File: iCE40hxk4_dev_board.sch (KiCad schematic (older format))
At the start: 0 parts

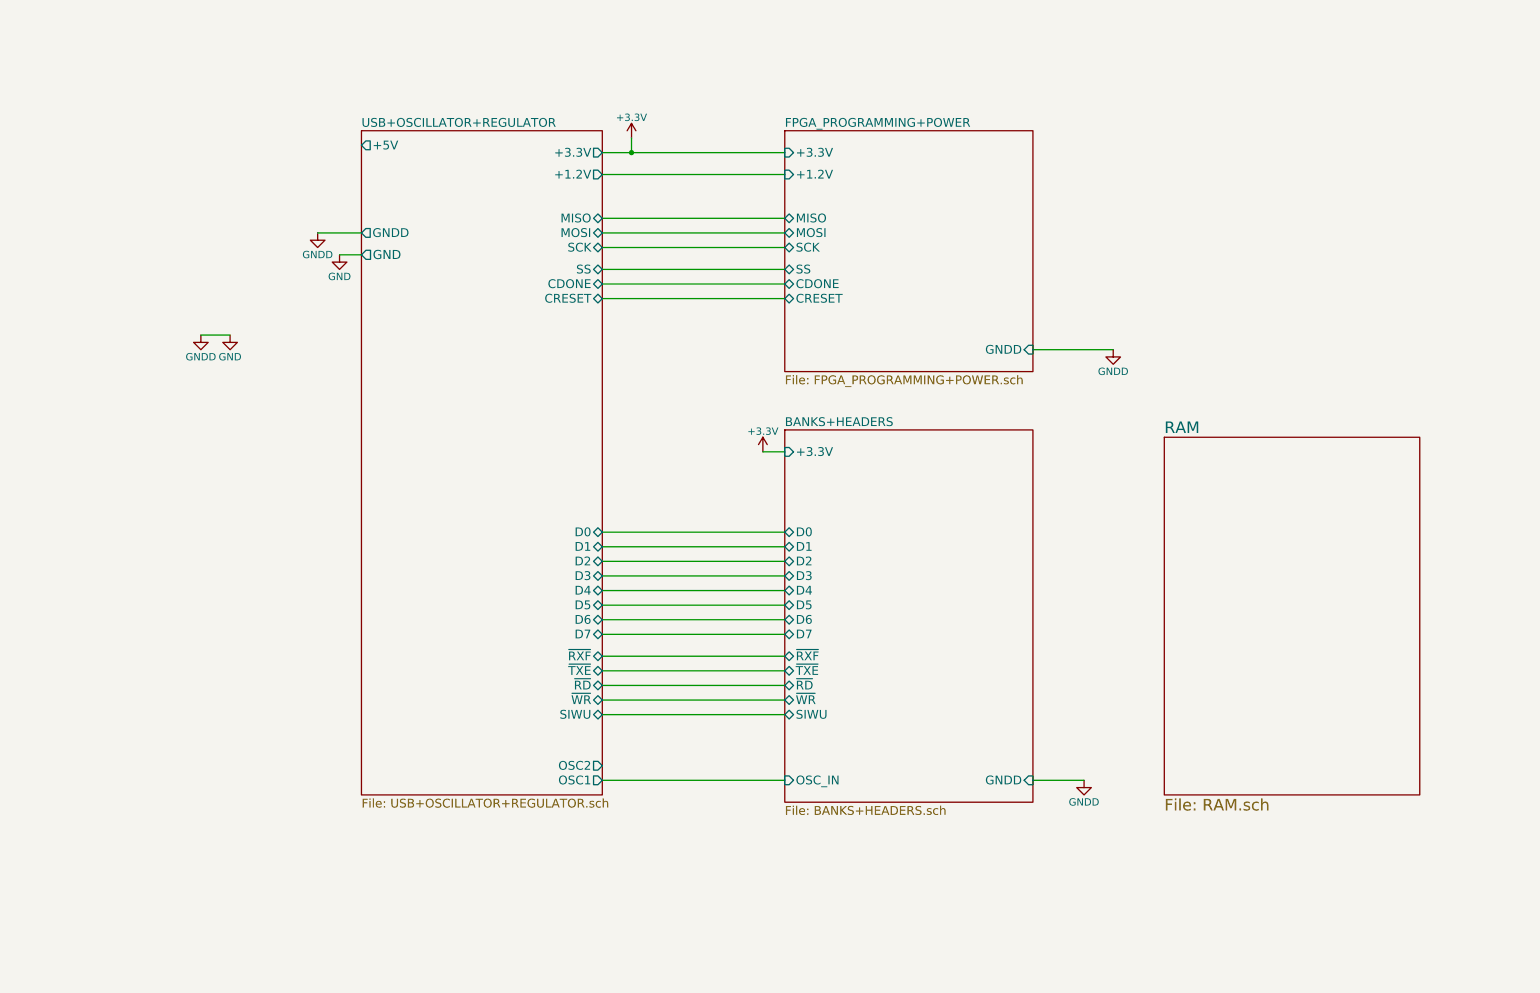
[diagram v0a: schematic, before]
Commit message: Reordered connections again. Option 1: RAM at left bank, some connections at left and top banks.
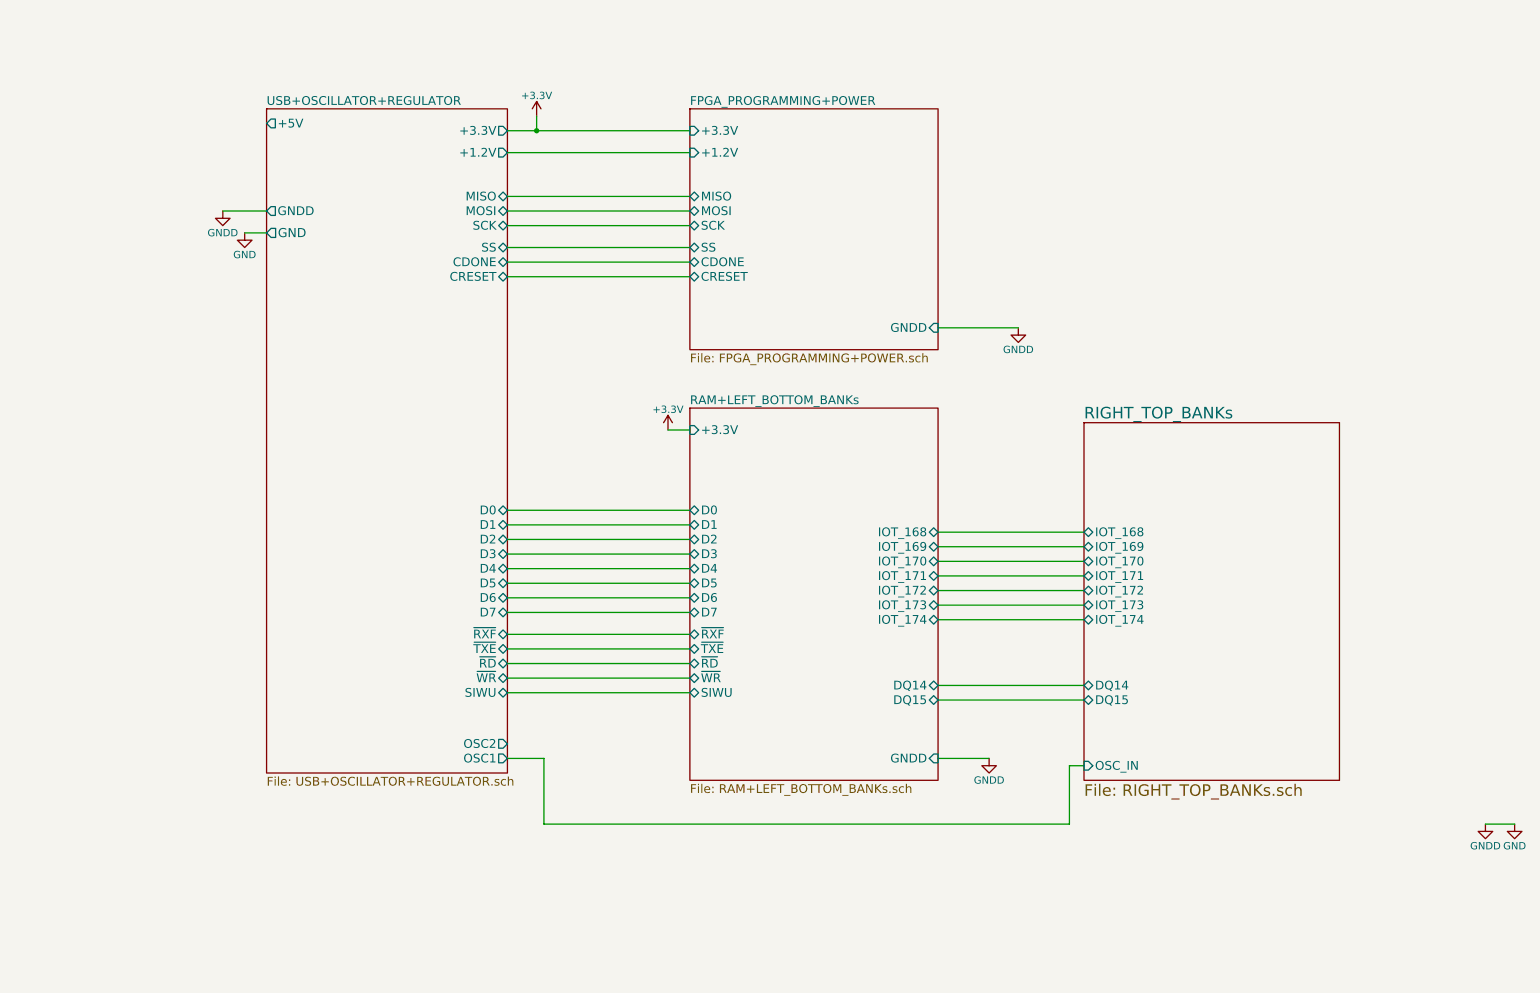
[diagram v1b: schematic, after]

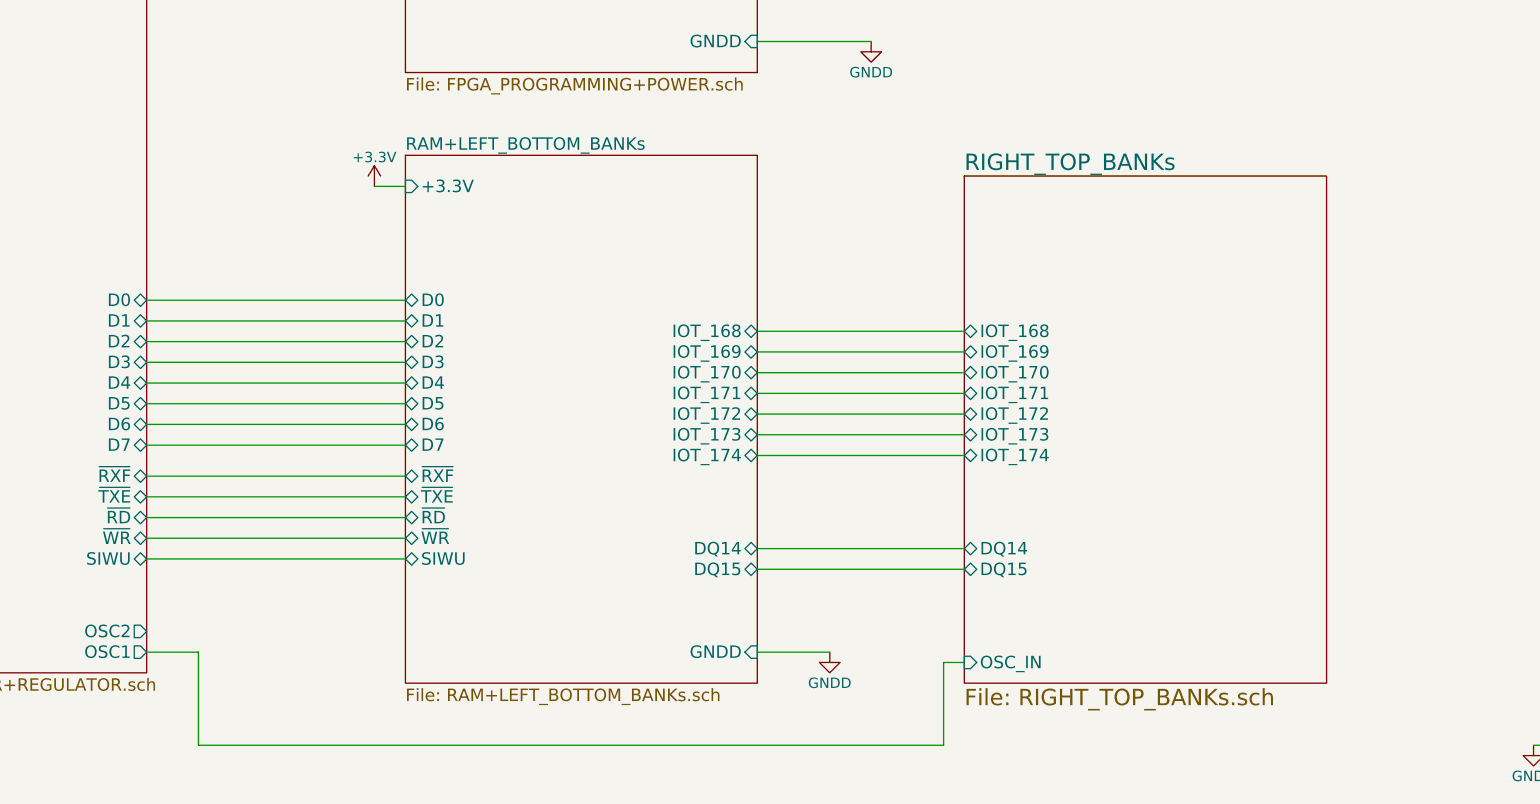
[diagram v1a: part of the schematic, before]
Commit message: The schematic is now free of any ERC error. Not connected and power flags added. No more global power pins, hierarchical labels used for power connections. TODO list: -Check if all footpritns are already assigned. -Export a BOM list, and check if all part numbers are assigned. -Add leds and testpoints. -Make another branch, with the RAM connections to the left and right banks, so the ram could be located in the bottom layer and the FPGA in the top layer. -Reorder the connections of the current branch if necessary, do the placement of components and ground planes.
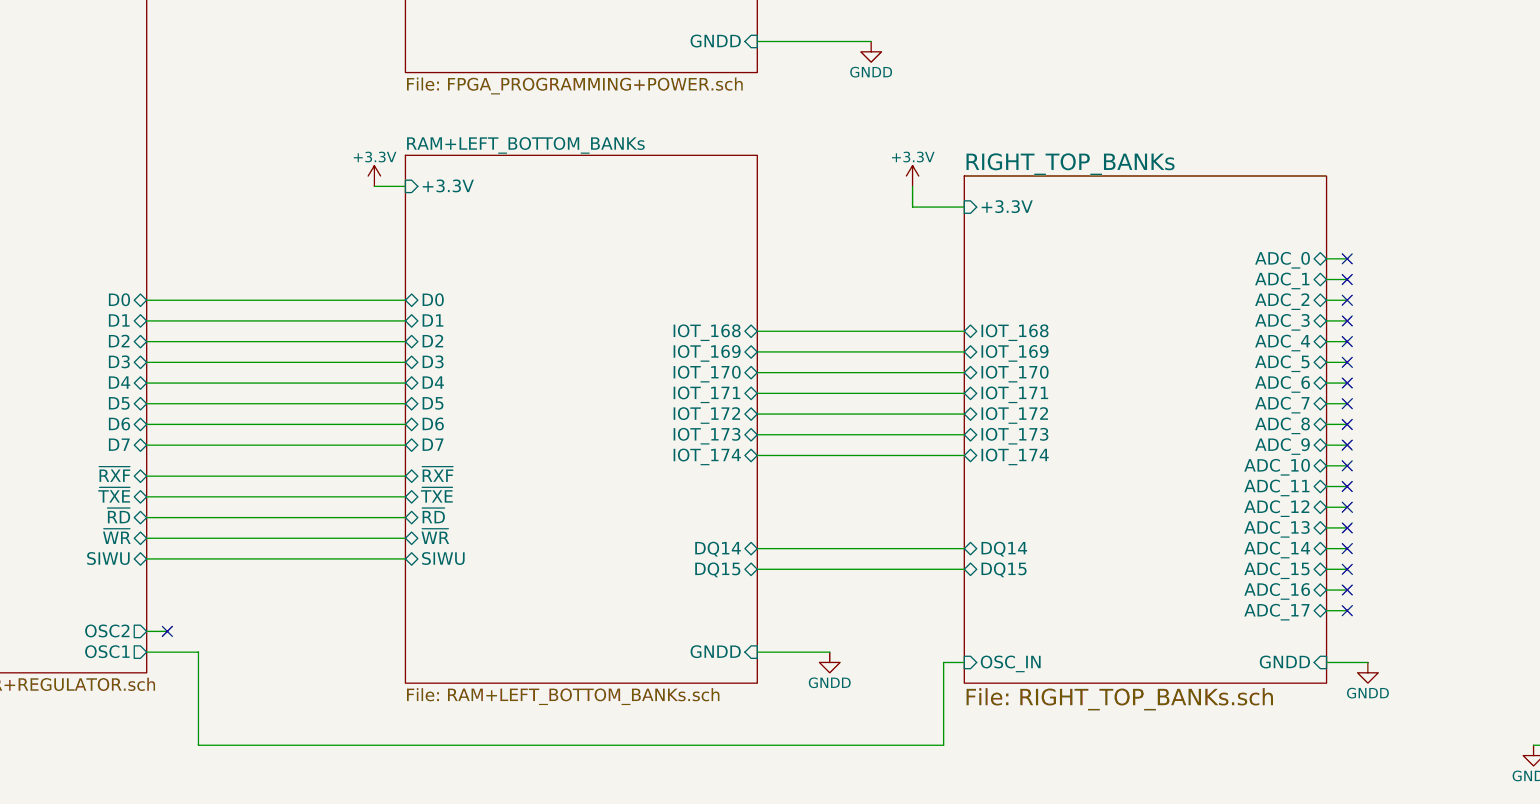
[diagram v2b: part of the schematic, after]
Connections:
- no-connect marks 0 -> 19
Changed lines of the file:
@@
 F10 "DQ15" B L 7850 5250 60
 F11 "DQ14" B L 7850 5150 60
+F12 "ADC_0" B R 9600 3750 60
+F13 "ADC_1" B R 9600 3850 60
+F14 "ADC_2" B R 9600 3950 60
+F15 "ADC_3" B R 9600 4050 60
+F16 "ADC_4" B R 9600 4150 60
+F17 "ADC_5" B R 9600 4250 60
+F18 "ADC_6" B R 9600 4350 60
+F19 "ADC_7" B R 9600 4450 60
+F20 "ADC_8" B R 9600 4550 60
+F21 "ADC_9" B R 9600 4650 60
+F22 "ADC_10" B R 9600 4750 60
+F23 "ADC_11" B R 9600 4850 60
+F24 "ADC_12" B R 9600 4950 60
+F25 "ADC_13" B R 9600 5050 60
+F26 "ADC_14" B R 9600 5150 60
+F27 "ADC_15" B R 9600 5250 60
+F28 "ADC_16" B R 9600 5350 60
+F29 "ADC_17" B R 9600 5450 60
+F30 "+3.3V" I L 7850 3500 60
+F31 "GNDD" I R 9600 5700 60
 $EndSheet
 Wire Wire Line
@@
 Wire Wire Line
 	6850 5150 7850 5150
+Wire Wire Line
+	9600 3750 9700 3750
+Wire Wire Line
+	9600 3850 9700 3850
+Wire Wire Line
+	9600 3950 9700 3950
+Wire Wire Line
+	9600 4050 9700 4050
+Wire Wire Line
+	9600 4150 9700 4150
+Wire Wire Line
+	9600 4250 9700 4250
+Wire Wire Line
+	9600 4350 9700 4350
+Wire Wire Line
+	9600 4450 9700 4450
+Wire Wire Line
+	9600 4550 9700 4550
+Wire Wire Line
+	9600 4650 9700 4650
+Wire Wire Line
+	9600 4750 9700 4750
+Wire Wire Line
+	9600 4850 9700 4850
+Wire Wire Line
+	9600 4950 9700 4950
+Wire Wire Line
+	9600 5050 9700 5050
+Wire Wire Line
+	9600 5150 9700 5150
+Wire Wire Line
+	9600 5250 9700 5250
+Wire Wire Line
+	9600 5350 9700 5350
+Wire Wire Line
+	9600 5450 9700 5450
+NoConn ~ 9700 3750
+NoConn ~ 9700 3850
+NoConn ~ 9700 3950
+NoConn ~ 9700 4050
+NoConn ~ 9700 4150
+NoConn ~ 9700 4250
+NoConn ~ 9700 4350
+NoConn ~ 9700 4450
+NoConn ~ 9700 4550
+NoConn ~ 9700 4650
+NoConn ~ 9700 4750
+NoConn ~ 9700 4850
+NoConn ~ 9700 4950
+NoConn ~ 9700 5050
+NoConn ~ 9700 5150
+NoConn ~ 9700 5250
+NoConn ~ 9700 5350
+NoConn ~ 9700 5450
+Wire Wire Line
+	3900 5550 4000 5550
+NoConn ~ 4000 5550
+$Comp
+L +3.3V #PWR09
+U 1 1 58F7EC7E
+P 7600 3400
+F 0 "#PWR09" H 7600 3250 50  0001 C CNN
+F 1 "+3.3V" H 7600 3540 50  0000 C CNN
+F 2 "" H 7600 3400 50  0001 C CNN
+F 3 "" H 7600 3400 50  0001 C CNN
+	1    7600 3400
+	1    0    0    -1
+$EndComp
+Wire Wire Line
+	7850 3500 7600 3500
+Wire Wire Line
+	7600 3500 7600 3400
+$Comp
+L GNDD #PWR010
+U 1 1 58F7F20A
+P 9800 5700
+F 0 "#PWR010" H 9800 5450 50  0001 C CNN
+F 1 "GNDD" H 9800 5550 50  0000 C CNN
+F 2 "" H 9800 5700 50  0001 C CNN
+F 3 "" H 9800 5700 50  0001 C CNN
+	1    9800 5700
+	1    0    0    -1
+$EndComp
+Wire Wire Line
+	9600 5700 9800 5700
 $EndSCHEMATC

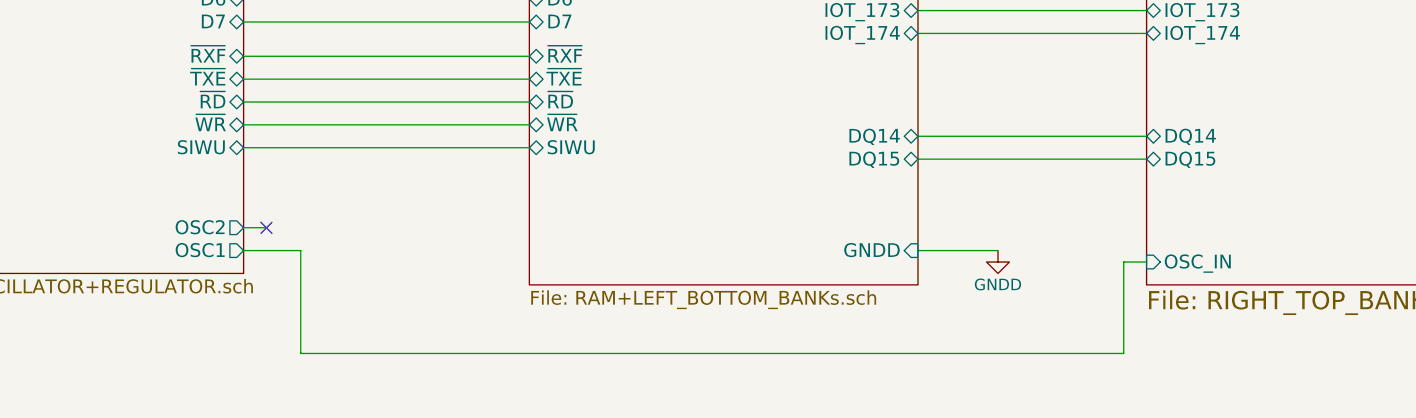
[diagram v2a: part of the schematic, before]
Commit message: Clk's buffers were removed and pcb routing was started
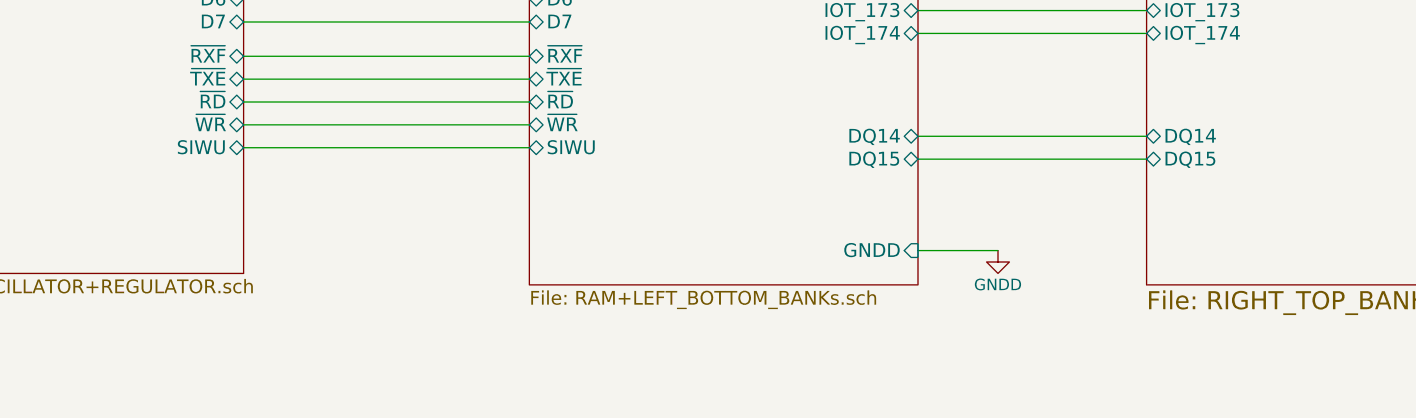
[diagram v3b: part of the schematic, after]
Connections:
- no-connect marks 19 -> 18
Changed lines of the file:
@@
 F5 "GND" O L 2250 2050 62
 F6 "GNDD" O L 2250 1900 60
-F7 "OSC1" O R 3900 5650 60
-F8 "OSC2" O R 3900 5550 60
-F9 "SCK" B R 3900 2000 60
-F10 "MOSI" B R 3900 1900 60
-F11 "MISO" B R 3900 1800 60
-F12 "SS" B R 3900 2150 60
-F13 "CDONE" B R 3900 2250 60
-F14 "CRESET" B R 3900 2350 60
-F15 "D0" B R 3900 3950 60
-F16 "D1" B R 3900 4050 60
-F17 "D2" B R 3900 4150 60
-F18 "D3" B R 3900 4250 60
-F19 "D4" B R 3900 4350 60
-F20 "D5" B R 3900 4450 60
-F21 "D6" B R 3900 4550 60
-F22 "D7" B R 3900 4650 60
-F23 "~RXF" B R 3900 4800 60
-F24 "~TXE" B R 3900 4900 60
-F25 "~RD" B R 3900 5000 60
-F26 "~WR" B R 3900 5100 60
-F27 "SIWU" B R 3900 5200 60
+F7 "SCK" B R 3900 2000 60
+F8 "MOSI" B R 3900 1900 60
+F9 "MISO" B R 3900 1800 60
+F10 "SS" B R 3900 2150 60
+F11 "CDONE" B R 3900 2250 60
+F12 "CRESET" B R 3900 2350 60
+F13 "D0" B R 3900 3950 60
+F14 "D1" B R 3900 4050 60
+F15 "D2" B R 3900 4150 60
+F16 "D3" B R 3900 4250 60
+F17 "D4" B R 3900 4350 60
+F18 "D5" B R 3900 4450 60
+F19 "D6" B R 3900 4550 60
+F20 "D7" B R 3900 4650 60
+F21 "~RXF" B R 3900 4800 60
+F22 "~TXE" B R 3900 4900 60
+F23 "~RD" B R 3900 5000 60
+F24 "~WR" B R 3900 5100 60
+F25 "SIWU" B R 3900 5200 60
 $EndSheet
 $Sheet
@@
 F0 "RIGHT_TOP_BANKs" 79
 F1 "RIGHT_TOP_BANKs.sch" 79
-F2 "OSC_IN" I L 7850 5700 60
-F3 "IOT_168" B L 7850 4100 60
-F4 "IOT_169" B L 7850 4200 60
-F5 "IOT_170" B L 7850 4300 60
-F6 "IOT_171" B L 7850 4400 60
-F7 "IOT_172" B L 7850 4500 60
-F8 "IOT_173" B L 7850 4600 60
-F9 "IOT_174" B L 7850 4700 60
-F10 "DQ15" B L 7850 5250 60
-F11 "DQ14" B L 7850 5150 60
-F12 "ADC_0" B R 9600 3750 60
-F13 "ADC_1" B R 9600 3850 60
-F14 "ADC_2" B R 9600 3950 60
-F15 "ADC_3" B R 9600 4050 60
-F16 "ADC_4" B R 9600 4150 60
-F17 "ADC_5" B R 9600 4250 60
-F18 "ADC_6" B R 9600 4350 60
-F19 "ADC_7" B R 9600 4450 60
-F20 "ADC_8" B R 9600 4550 60
-F21 "ADC_9" B R 9600 4650 60
-F22 "ADC_10" B R 9600 4750 60
-F23 "ADC_11" B R 9600 4850 60
-F24 "ADC_12" B R 9600 4950 60
-F25 "ADC_13" B R 9600 5050 60
-F26 "ADC_14" B R 9600 5150 60
-F27 "ADC_15" B R 9600 5250 60
-F28 "ADC_16" B R 9600 5350 60
-F29 "ADC_17" B R 9600 5450 60
-F30 "+3.3V" I L 7850 3500 60
-F31 "GNDD" I R 9600 5700 60
+F2 "IOT_168" B L 7850 4100 60
+F3 "IOT_169" B L 7850 4200 60
+F4 "IOT_170" B L 7850 4300 60
+F5 "IOT_171" B L 7850 4400 60
+F6 "IOT_172" B L 7850 4500 60
+F7 "IOT_173" B L 7850 4600 60
+F8 "IOT_174" B L 7850 4700 60
+F9 "DQ15" B L 7850 5250 60
+F10 "DQ14" B L 7850 5150 60
+F11 "ADC_0" B R 9600 3750 60
+F12 "ADC_1" B R 9600 3850 60
+F13 "ADC_2" B R 9600 3950 60
+F14 "ADC_3" B R 9600 4050 60
+F15 "ADC_4" B R 9600 4150 60
+F16 "ADC_5" B R 9600 4250 60
+F17 "ADC_6" B R 9600 4350 60
+F18 "ADC_7" B R 9600 4450 60
+F19 "ADC_8" B R 9600 4550 60
+F20 "ADC_9" B R 9600 4650 60
+F21 "ADC_10" B R 9600 4750 60
+F22 "ADC_11" B R 9600 4850 60
+F23 "ADC_12" B R 9600 4950 60
+F24 "ADC_13" B R 9600 5050 60
+F25 "ADC_14" B R 9600 5150 60
+F26 "ADC_15" B R 9600 5250 60
+F27 "ADC_16" B R 9600 5350 60
+F28 "ADC_17" B R 9600 5450 60
+F29 "+3.3V" I L 7850 3500 60
+F30 "GNDD" I R 9600 5700 60
 $EndSheet
 Wire Wire Line
@@
 Wire Wire Line
 	6850 4700 7850 4700
-Wire Wire Line
-	3900 5650 4150 5650
-Wire Wire Line
-	4150 5650 4150 6100
-Wire Wire Line
-	4150 6100 7750 6100
-Wire Wire Line
-	7750 6100 7750 5700
-Wire Wire Line
-	7750 5700 7850 5700
 $Sheet
 S 5150 3250 1700 2550
@@
 NoConn ~ 9700 5350
 NoConn ~ 9700 5450
-Wire Wire Line
-	3900 5550 4000 5550
-NoConn ~ 4000 5550
 $Comp
 L +3.3V #PWR09
